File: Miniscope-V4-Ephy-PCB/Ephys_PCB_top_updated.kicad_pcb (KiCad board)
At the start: 2 copper layers, 41 parts, among them J1 34 Circuit Slimslack Connector, J10 Conn_01x01, J11 Conn_01x01, J12 Conn_01x01, J13 Conn_01x01, J4 Conn_01x01, J5 Conn_01x01, J8 Conn_01x01, U1 ATSAME70N21A-CN, U2 RHD2132_QFN-RHD2132, U3 TLV7103318DSER, U4 TXB0304RUT, Y1 ABM8G-12.000MHZ-4Y-T3

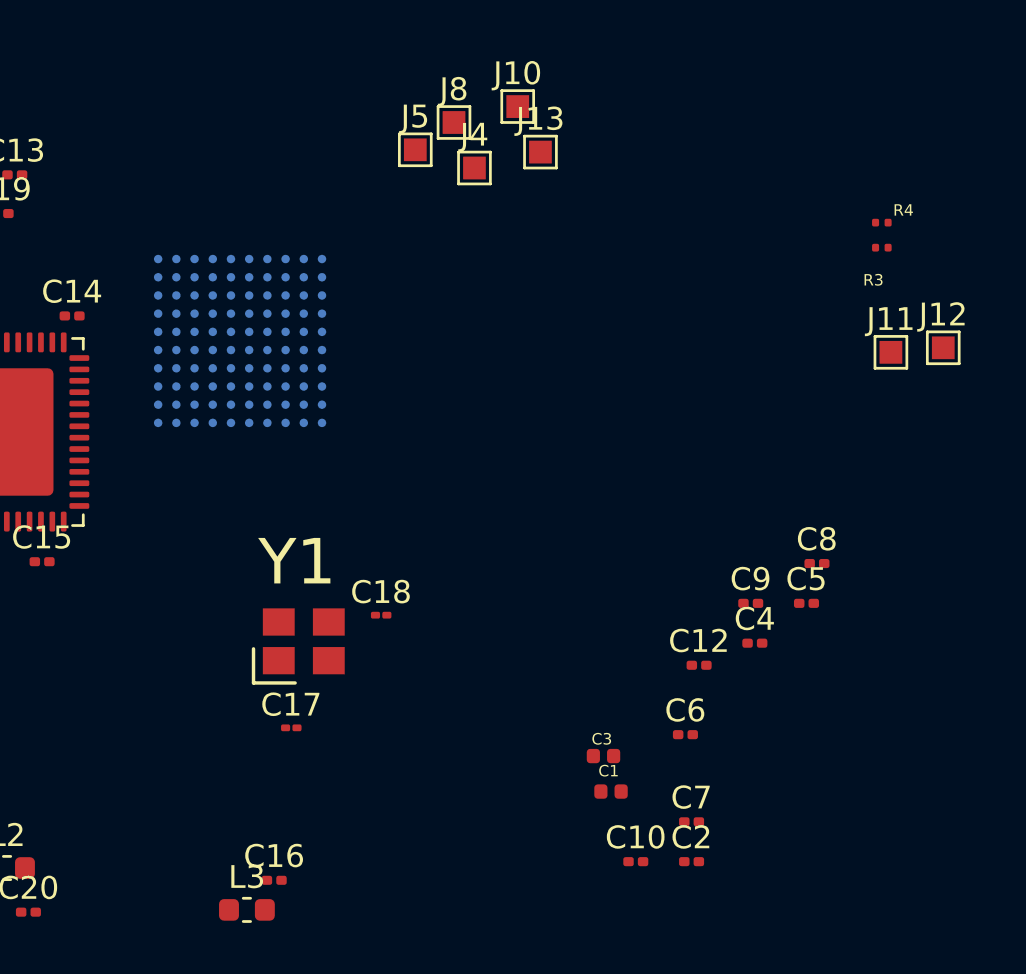
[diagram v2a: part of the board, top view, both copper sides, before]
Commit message: Update Board Setup Specifications
Via: 0.15mm/0,3mm
Trace/Space: 3mil/3mil
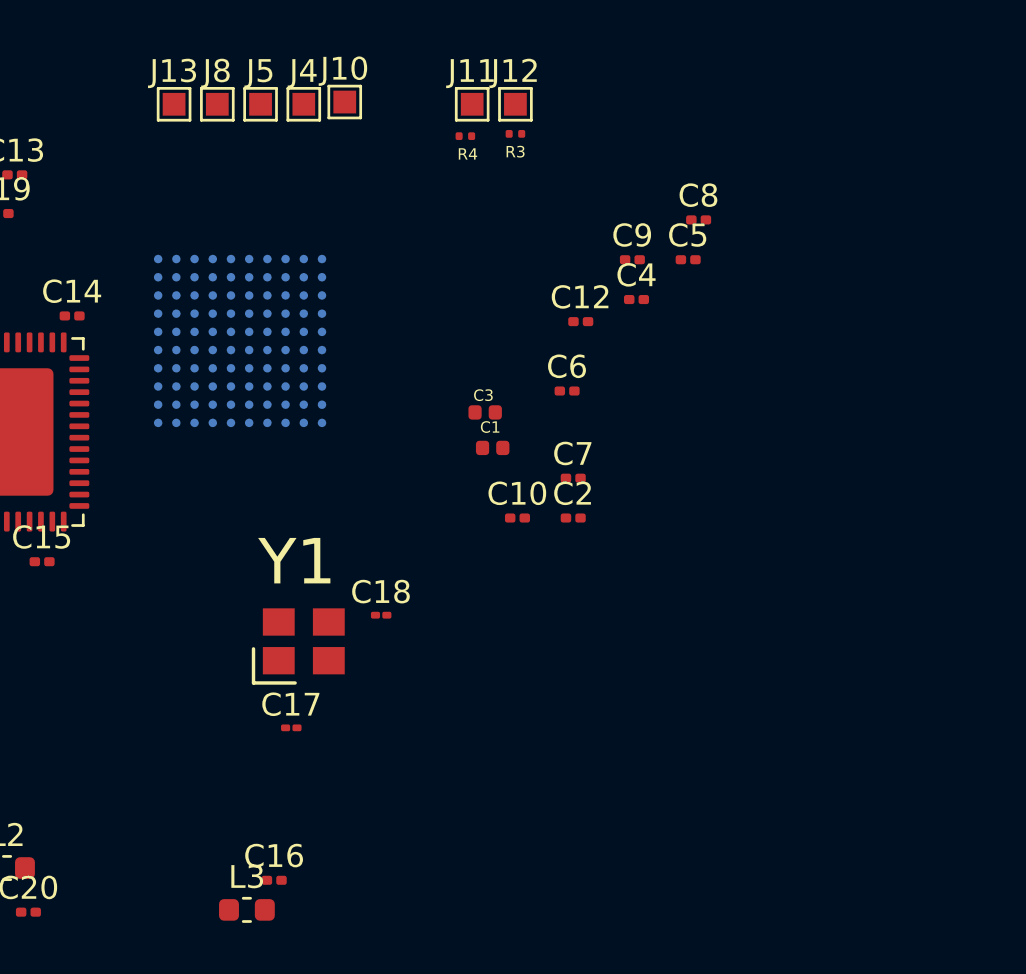
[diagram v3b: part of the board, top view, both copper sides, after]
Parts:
- moved J12 21.6 mm to (155.6, 75.3)
- moved J11 21.4 mm to (153.7, 75.3)
- moved R4 18.7 mm to (153.4, 76.7)
- moved R3 16.9 mm to (155.6, 76.6)
- moved J13 16.2 mm to (140.6, 75.3)
- moved C4 16.0 mm to (160.9, 83.9)
- moved C12 16.0 mm to (158.5, 84.8)
- moved C5 16.0 mm to (163.2, 82.1)
- moved C8 16.0 mm to (163.7, 80.4)
- moved C9 16.0 mm to (160.7, 82.1)
- moved C1 16.0 mm to (154.6, 90.4)
- moved C2 16.0 mm to (158.1, 93.5)
- moved C7 16.0 mm to (158.1, 91.7)
- moved C10 16.0 mm to (155.7, 93.5)
- moved C3 16.0 mm to (154.3, 88.8)
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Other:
- net class Default: clearance 0.2 -> 0.0762; trace_width 0.25 -> 0.0762; via_dia 0.8 -> 0.3; via_drill 0.4 -> 0.15
- rule trace_clearance: 0.2 -> 0.0762
- rule trace_min: 0.2 -> 0.0762
- rule via_min_drill: 0.3 -> 0.15
- rule via_min_size: 0.4 -> 0.3
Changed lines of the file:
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@@
   )
   (setup
-    (last_trace_width 0.25)
-    (trace_clearance 0.2)
+    (last_trace_width 0.0762)
+    (user_trace_width 0.0762)
+    (user_trace_width 0.1016)
+    (user_trace_width 0.127)
+    (user_trace_width 0.1524)
+    (user_trace_width 0.2032)
+    (user_trace_width 0.254)
+    (user_trace_width 0.3048)
+    (trace_clearance 0.0762)
     (zone_clearance 0.508)
     (zone_45_only no)
-    (trace_min 0.2)
-    (via_size 0.8)
-    (via_drill 0.4)
-    (via_min_size 0.4)
-    (via_min_drill 0.3)
+    (trace_min 0.0762)
+    (via_size 0.3)
+    (via_drill 0.15)
+    (via_min_size 0.3)
+    (via_min_drill 0.15)
+    (user_via 0.3 0.15)
+    (user_via 0.35 0.15)
     (uvia_size 0.3)
     (uvia_drill 0.1)
@@
     (mod_text_size 1 1)
     (mod_text_width 0.15)
-    (pad_size 1.524 1.524)
-    (pad_drill 0.762)
+    (pad_size 5.6 5.6)
+    (pad_drill 0)
     (pad_to_mask_clearance 0)
     (aux_axis_origin 0 0)
@@
   (net 136 "Net-(D1-Pad1)")
   (net_class Default "This is the default net class."
-    (clearance 0.2)
-    (trace_width 0.25)
-    (via_dia 0.8)
-    (via_drill 0.4)
+    (clearance 0.0762)
+    (trace_width 0.0762)
+    (via_dia 0.3)
+    (via_drill 0.15)
     (uvia_dia 0.3)
     (uvia_drill 0.1)
@@
   )
   (module .Resistor:R_0201_0603Metric_ERJ_L (layer F.Cu)
-    (at 171.7 80.5)
+    (at 153.4 76.7)
     (descr "Resistor, Chip; 0.60 mm L X 0.30 mm W X 0.26 mm H body")
     (attr smd)
@@
     (fp_line (start -0.15 0.15) (end -0.3 0.15) (layer Dwgs.User) (width 0.025))
     (fp_line (start -0.15 -0.15) (end -0.15 0.15) (layer Dwgs.User) (width 0.025))
-    (fp_text user %R (at 0.95 -0.54) (layer F.SilkS)
+    (fp_text user %R (at 0.1 0.8) (layer F.SilkS)
       (effects (font (size 0.5 0.5) (thickness 0.05)))
     )
@@
   )
   (module .Resistor:R_0201_0603Metric_ERJ_L (layer F.Cu)
-    (at 171.7 81.6)
+    (at 155.6 76.6)
     (descr "Resistor, Chip; 0.60 mm L X 0.30 mm W X 0.26 mm H body")
     (attr smd)
@@
     (fp_line (start -0.15 0.15) (end -0.3 0.15) (layer Dwgs.User) (width 0.025))
     (fp_line (start -0.15 -0.15) (end -0.15 0.15) (layer Dwgs.User) (width 0.025))
-    (fp_text user %R (at -0.37 1.43) (layer F.SilkS)
+    (fp_text user %R (at 0 0.8) (layer F.SilkS)
       (effects (font (size 0.5 0.5) (thickness 0.05)))
     )
@@
   )
   (module TestPoint:TestPoint_Pad_1.0x1.0mm (layer F.Cu)
-    (at 156.7 77.4)
+    (at 140.6 75.3)
     (descr "SMD rectangular pad as test Point, square 1.0mm side length")
     (tags "test point SMD pad rectangle square")
@@
   )
   (module TestPoint:TestPoint_Pad_1.0x1.0mm (layer F.Cu)
-    (at 174.4 86)
+    (at 155.6 75.3)
     (descr "SMD rectangular pad as test Point, square 1.0mm side length")
     (tags "test point SMD pad rectangle square")
@@
   )
   (module TestPoint:TestPoint_Pad_1.0x1.0mm (layer F.Cu)
-    (at 172.1 86.2)
+    (at 153.7 75.3)
     (descr "SMD rectangular pad as test Point, square 1.0mm side length")
     (tags "test point SMD pad rectangle square")
@@
   )
   (module TestPoint:TestPoint_Pad_1.0x1.0mm (layer F.Cu)
-    (at 155.7 75.4)
+    (at 148.1 75.2)
     (descr "SMD rectangular pad as test Point, square 1.0mm side length")
     (tags "test point SMD pad rectangle square")
@@
   )
   (module TestPoint:TestPoint_Pad_1.0x1.0mm (layer F.Cu)
-    (at 152.9 76.1)
+    (at 142.5 75.3)
     (descr "SMD rectangular pad as test Point, square 1.0mm side length")
     (tags "test point SMD pad rectangle square")
@@
   )
   (module TestPoint:TestPoint_Pad_1.0x1.0mm (layer F.Cu)
-    (at 151.2 77.3)
+    (at 144.4 75.3)
     (descr "SMD rectangular pad as test Point, square 1.0mm side length")
     (tags "test point SMD pad rectangle square")
@@
   )
   (module TestPoint:TestPoint_Pad_1.0x1.0mm (layer F.Cu)
-    (at 153.8 78.1)
+    (at 146.3 75.3)
     (descr "SMD rectangular pad as test Point, square 1.0mm side length")
     (tags "test point SMD pad rectangle square")
@@
   )
   (module Capacitor_SMD:C_0201_0603Metric (layer F.Cu)
-    (at 163.67 99.95)
+    (at 158.47 84.85)
     (descr "Capacitor SMD 0201 (0603 Metric), square (rectangular) end terminal, IPC_7351 nominal, (Body size source: https://www.vishay.com/docs/20052/crcw0201e3.pdf), generated with kicad-footprint-generator")
     (tags capacitor)
@@
   )
   (module Capacitor_SMD:C_0201_0603Metric (layer F.Cu)
-    (at 160.89 108.58)
+    (at 155.69 93.48)
     (descr "Capacitor SMD 0201 (0603 Metric), square (rectangular) end terminal, IPC_7351 nominal, (Body size source: https://www.vishay.com/docs/20052/crcw0201e3.pdf), generated with kicad-footprint-generator")
     (tags capacitor)
@@
   )
   (module Capacitor_SMD:C_0201_0603Metric (layer F.Cu)
-    (at 165.94 97.23)
+    (at 160.74 82.13)
     (descr "Capacitor SMD 0201 (0603 Metric), square (rectangular) end terminal, IPC_7351 nominal, (Body size source: https://www.vishay.com/docs/20052/crcw0201e3.pdf), generated with kicad-footprint-generator")
     (tags capacitor)
@@
   )
   (module Capacitor_SMD:C_0201_0603Metric (layer F.Cu)
-    (at 168.85 95.48)
+    (at 163.65 80.38)
     (descr "Capacitor SMD 0201 (0603 Metric), square (rectangular) end terminal, IPC_7351 nominal, (Body size source: https://www.vishay.com/docs/20052/crcw0201e3.pdf), generated with kicad-footprint-generator")
     (tags capacitor)
@@
   )
   (module Capacitor_SMD:C_0201_0603Metric (layer F.Cu)
-    (at 163.34 106.83)
+    (at 158.14 91.73)
     (descr "Capacitor SMD 0201 (0603 Metric), square (rectangular) end terminal, IPC_7351 nominal, (Body size source: https://www.vishay.com/docs/20052/crcw0201e3.pdf), generated with kicad-footprint-generator")
     (tags capacitor)
@@
   )
   (module Capacitor_SMD:C_0201_0603Metric (layer F.Cu)
-    (at 163.07 103)
+    (at 157.87 87.9)
     (descr "Capacitor SMD 0201 (0603 Metric), square (rectangular) end terminal, IPC_7351 nominal, (Body size source: https://www.vishay.com/docs/20052/crcw0201e3.pdf), generated with kicad-footprint-generator")
     (tags capacitor)
@@
   )
   (module Capacitor_SMD:C_0201_0603Metric (layer F.Cu)
-    (at 168.39 97.23)
+    (at 163.19 82.13)
     (descr "Capacitor SMD 0201 (0603 Metric), square (rectangular) end terminal, IPC_7351 nominal, (Body size source: https://www.vishay.com/docs/20052/crcw0201e3.pdf), generated with kicad-footprint-generator")
     (tags capacitor)
@@
   )
   (module Capacitor_SMD:C_0201_0603Metric (layer F.Cu)
-    (at 166.12 98.98)
+    (at 160.92 83.88)
     (descr "Capacitor SMD 0201 (0603 Metric), square (rectangular) end terminal, IPC_7351 nominal, (Body size source: https://www.vishay.com/docs/20052/crcw0201e3.pdf), generated with kicad-footprint-generator")
     (tags capacitor)
@@
   )
   (module .Capacitor:C_0402_1005Metric_L (layer F.Cu)
-    (at 159.47 103.94)
+    (at 154.27 88.84)
     (descr "Capacitor, Chip; 1.00 mm L X 0.50 mm W X 0.65 mm H body")
     (attr smd)
@@
   )
   (module Capacitor_SMD:C_0201_0603Metric (layer F.Cu)
-    (at 163.34 108.58)
+    (at 158.14 93.48)
     (descr "Capacitor SMD 0201 (0603 Metric), square (rectangular) end terminal, IPC_7351 nominal, (Body size source: https://www.vishay.com/docs/20052/crcw0201e3.pdf), generated with kicad-footprint-generator")
     (tags capacitor)
@@
   )
   (module .Capacitor:C_0402_1005Metric_L (layer F.Cu)
-    (at 159.8 105.5)
+    (at 154.6 90.4)
     (descr "Capacitor, Chip; 1.00 mm L X 0.50 mm W X 0.65 mm H body")
     (attr smd)

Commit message: Switch to 6 layer PCB
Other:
- copper layers 2 -> 6
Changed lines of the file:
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@@
 (kicad_pcb (version 20171130) (host pcbnew "(5.1.5)-3")
   (general
-    (thickness 1.6)
+    (thickness 0.8)
     (drawings 0)
     (tracks 0)
@@
   (layers
     (0 F.Cu signal)
+    (1 In1.Cu signal)
+    (2 In2.Cu signal)
+    (3 In3.Cu signal)
+    (4 In4.Cu signal)
     (31 B.Cu signal)
     (32 B.Adhes user)
@@
     (38 B.Mask user)
     (39 F.Mask user)
-    (40 Dwgs.User user hide)
+    (40 Dwgs.User user)
     (41 Cmts.User user)
     (42 Eco1.User user)
@@
     (46 B.CrtYd user hide)
     (47 F.CrtYd user hide)
-    (48 B.Fab user)
+    (48 B.Fab user hide)
     (49 F.Fab user hide)
   )
   (setup
-    (last_trace_width 0.0762)
+    (last_trace_width 0.1016)
     (user_trace_width 0.0762)
     (user_trace_width 0.1016)

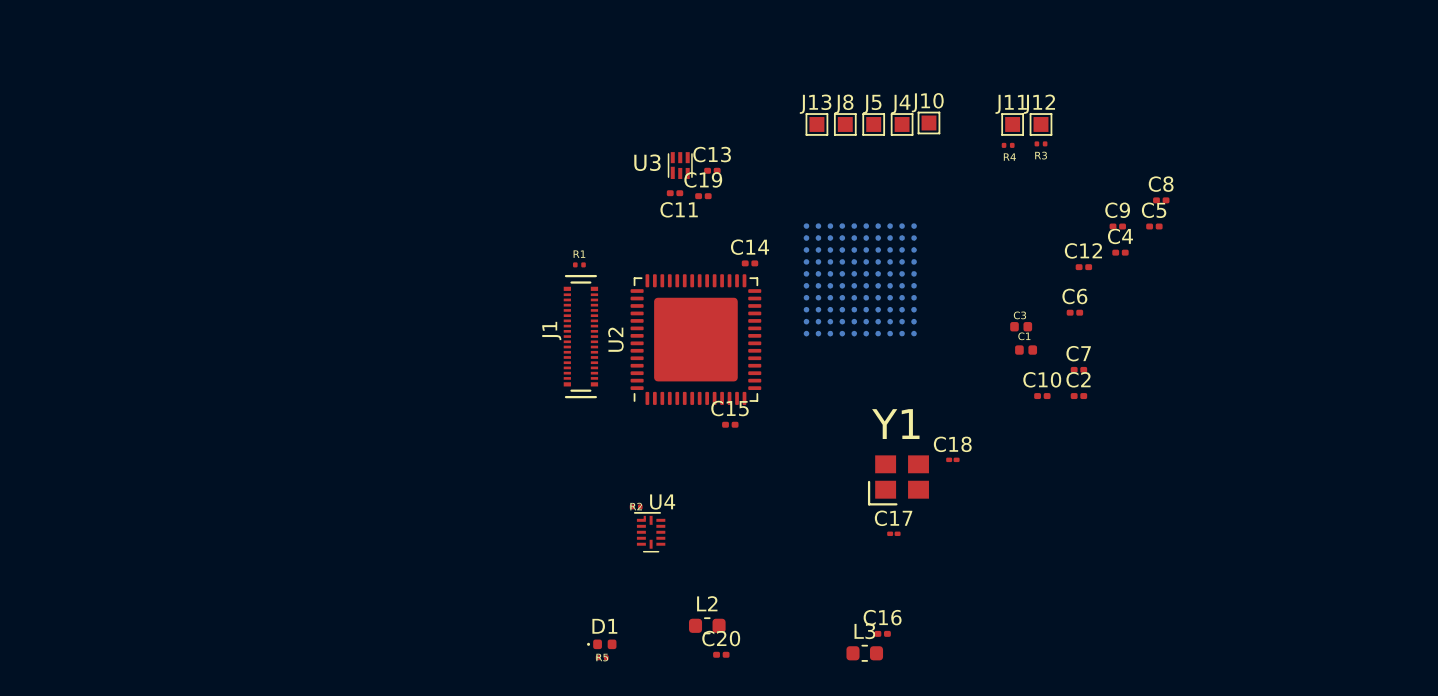
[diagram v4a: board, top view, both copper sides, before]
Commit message: Move things around in PCBnew and add prelim board outline.
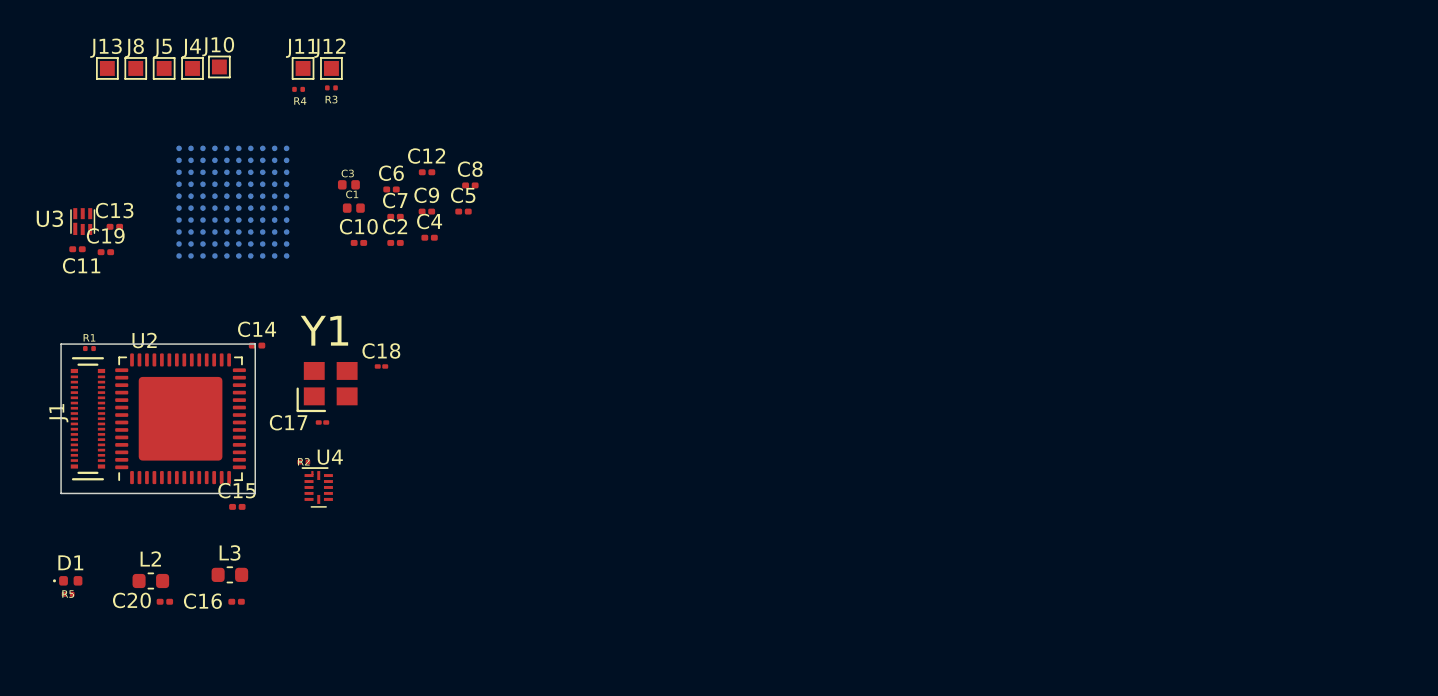
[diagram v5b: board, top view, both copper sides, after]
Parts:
- moved J4 47.6 mm to (98.8, 71.5)
- moved J10 47.6 mm to (100.6, 71.5)
- moved J12 47.6 mm to (108.1, 71.5)
- moved J13 47.6 mm to (93.1, 71.5)
- moved J5 47.6 mm to (96.9, 71.5)
- moved J8 47.6 mm to (95.0, 71.5)
- moved R3 47.6 mm to (108.1, 72.8)
- moved R4 47.6 mm to (105.9, 73.0)
- moved J11 47.6 mm to (106.2, 71.5)
- moved C10 46.9 mm to (109.9, 83.2)
- moved C2 46.9 mm to (112.4, 83.2)
- moved C7 46.9 mm to (112.4, 81.5)
- moved C6 46.5 mm to (112.1, 79.7)
- moved C9 46.3 mm to (114.5, 81.1)
- moved C5 46.3 mm to (116.9, 81.1)
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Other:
- board outline added: 13 x 10 mm

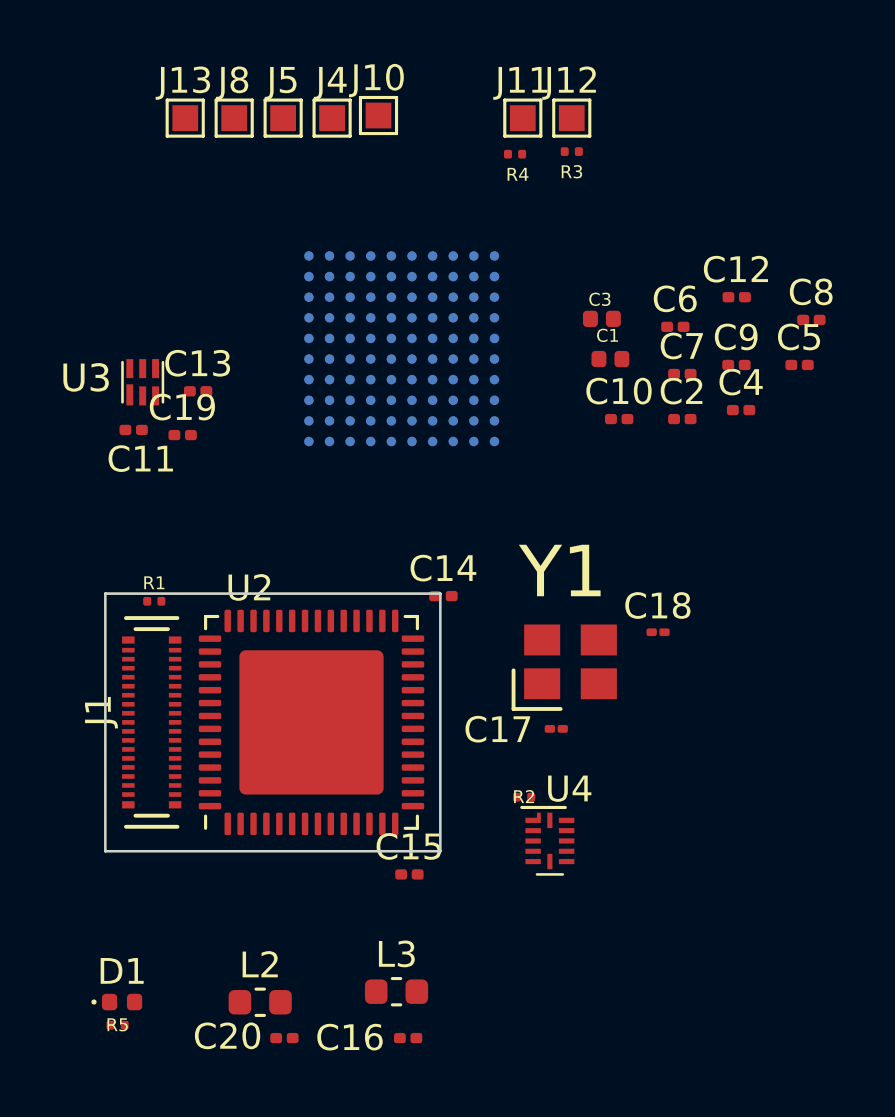
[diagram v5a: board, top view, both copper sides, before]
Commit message: Change display layers for designators and footprint info.
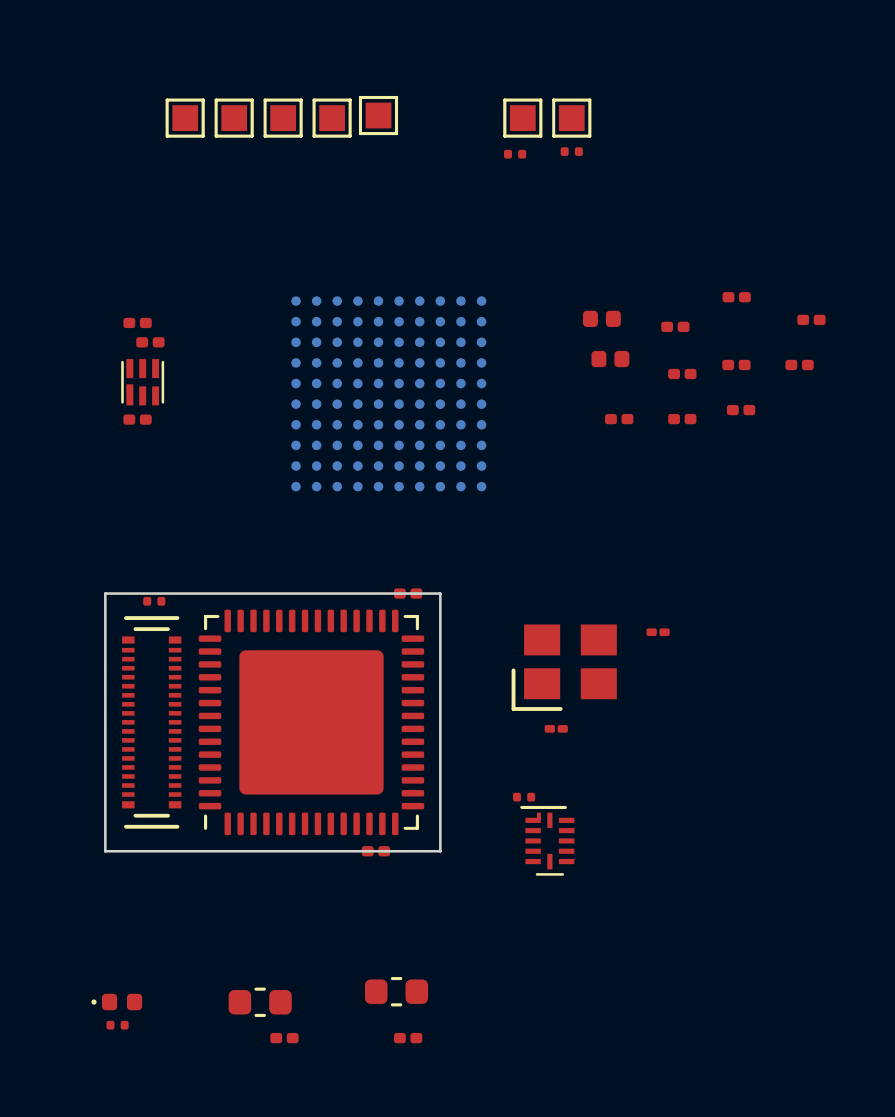
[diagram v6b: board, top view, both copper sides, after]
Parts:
- moved C19 4.69 mm to (91.2, 79.5)
- moved C13 2.65 mm to (91.8, 80.2)
- moved U1 1.82 mm to (101.0, 82.2)
- moved C15 1.58 mm to (100.5, 100.0), turned to 180 degrees
- moved C14 1.37 mm to (101.8, 90.0), turned to 180 degrees
- moved C11 0.43 mm to (91.2, 83.2)
